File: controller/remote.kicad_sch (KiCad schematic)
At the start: 11 parts, among them J1 Conn_01x03, U6 MC130VX

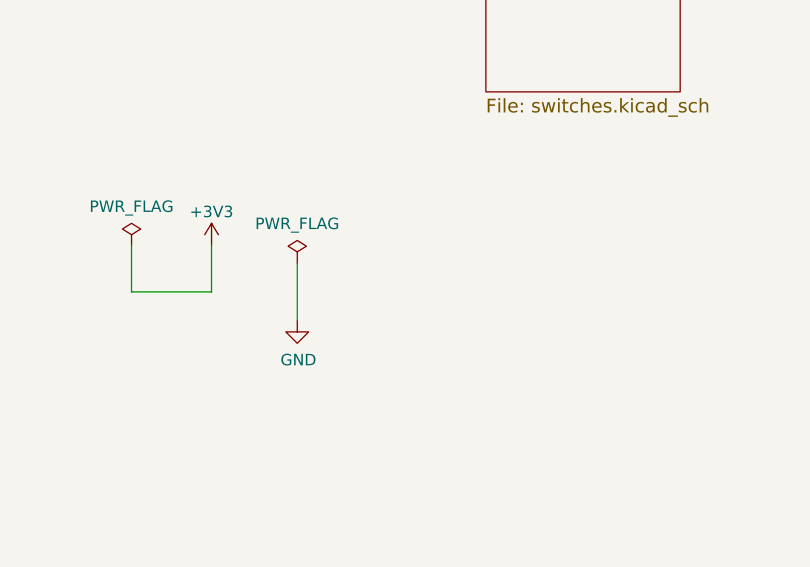
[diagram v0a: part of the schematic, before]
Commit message: Add debug connector.
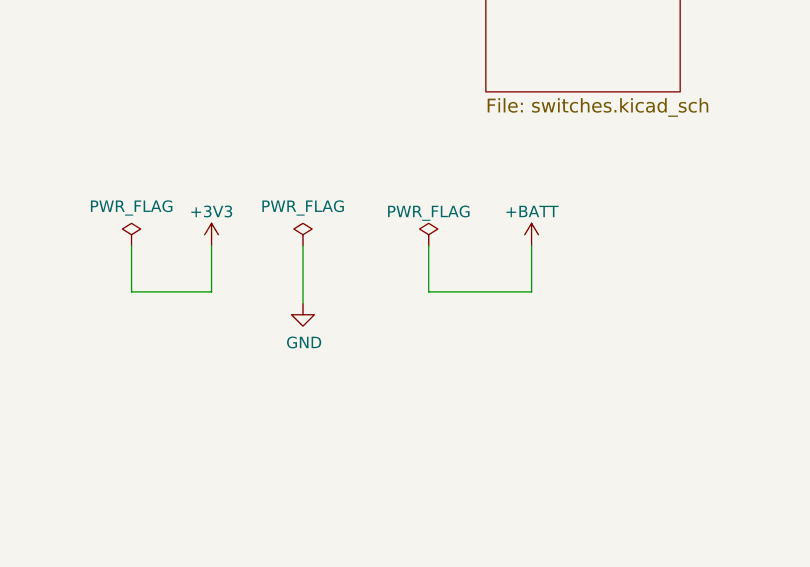
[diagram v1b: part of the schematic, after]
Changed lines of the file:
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@@
     (stroke (width 0) (type default))
   )
-  (wire (pts (xy 123.825 66.675) (xy 123.825 60.325))
+  (wire (pts (xy 149.86 63.5) (xy 138.43 63.5))
+    (stroke (width 0) (type default))
+  )
+  (wire (pts (xy 124.46 64.77) (xy 124.46 58.42))
     (stroke (width 0) (type default))
   )
@@
     (stroke (width 0) (type default))
   )
+  (wire (pts (xy 149.86 58.42) (xy 149.86 63.5))
+    (stroke (width 0) (type default))
+  )
   (wire (pts (xy 41.91 86.36) (xy 41.91 96.52))
     (stroke (width 0) (type default))
@@
   )
   (wire (pts (xy 41.91 45.72) (xy 46.99 45.72))
+    (stroke (width 0) (type default))
+  )
+  (wire (pts (xy 138.43 63.5) (xy 138.43 58.42))
     (stroke (width 0) (type default))
   )
@@
     )
   )
-  (symbol (lib_id "power:PWR_FLAG") (at 123.825 60.325 0) (unit 1)
-    (in_bom yes) (on_board yes) (dnp no)
-    (property "Reference" "#FLG0102" (at 123.825 58.42 0)
-      (effects (font (size 1.27 1.27)) hide)
-    )
-    (property "Value" "PWR_FLAG" (at 123.825 55.9308 0)
-      (effects (font (size 1.27 1.27)))
-    )
-    (property "Footprint" "" (at 123.825 60.325 0)
-      (effects (font (size 1.27 1.27)) hide)
-    )
-    (property "Datasheet" "~" (at 123.825 60.325 0)
+  (symbol (lib_id "power:PWR_FLAG") (at 124.46 58.42 0) (unit 1)
+    (in_bom yes) (on_board yes) (dnp no)
+    (property "Reference" "#FLG0102" (at 124.46 56.515 0)
+      (effects (font (size 1.27 1.27)) hide)
+    )
+    (property "Value" "PWR_FLAG" (at 124.46 54.0258 0)
+      (effects (font (size 1.27 1.27)))
+    )
+    (property "Footprint" "" (at 124.46 58.42 0)
+      (effects (font (size 1.27 1.27)) hide)
+    )
+    (property "Datasheet" "~" (at 124.46 58.42 0)
       (effects (font (size 1.27 1.27)) hide)
     )
@@
     )
   )
-  (symbol (lib_id "power:GND") (at 123.825 66.675 0) (unit 1)
-    (in_bom yes) (on_board yes) (dnp no)
-    (property "Reference" "#PWR0128" (at 123.825 73.025 0)
-      (effects (font (size 1.27 1.27)) hide)
-    )
-    (property "Value" "GND" (at 123.952 71.0692 0)
-      (effects (font (size 1.27 1.27)))
-    )
-    (property "Footprint" "" (at 123.825 66.675 0)
-      (effects (font (size 1.27 1.27)) hide)
-    )
-    (property "Datasheet" "" (at 123.825 66.675 0)
+  (symbol (lib_id "power:GND") (at 124.46 64.77 0) (unit 1)
+    (in_bom yes) (on_board yes) (dnp no)
+    (property "Reference" "#PWR0128" (at 124.46 71.12 0)
+      (effects (font (size 1.27 1.27)) hide)
+    )
+    (property "Value" "GND" (at 124.587 69.1642 0)
+      (effects (font (size 1.27 1.27)))
+    )
+    (property "Footprint" "" (at 124.46 64.77 0)
+      (effects (font (size 1.27 1.27)) hide)
+    )
+    (property "Datasheet" "" (at 124.46 64.77 0)
       (effects (font (size 1.27 1.27)) hide)
     )
@@
     )
   )
+  (symbol (lib_id "power:+BATT") (at 149.86 58.42 0) (unit 1)
+    (in_bom yes) (on_board yes) (dnp no) (fields_autoplaced)
+    (property "Reference" "#PWR019" (at 149.86 62.23 0)
+      (effects (font (size 1.27 1.27)) hide)
+    )
+    (property "Value" "+BATT" (at 149.86 54.61 0)
+      (effects (font (size 1.27 1.27)))
+    )
+    (property "Footprint" "" (at 149.86 58.42 0)
+      (effects (font (size 1.27 1.27)) hide)
+    )
+    (property "Datasheet" "" (at 149.86 58.42 0)
+      (effects (font (size 1.27 1.27)) hide)
+    )
+    (pin "1")
+    (instances
+      (project "remote"
+        (path "/0776e334-fbf5-4a46-a47e-c7e0521e2a6b"
+          (reference "#PWR019") (unit 1)
+        )
+      )
+    )
+  )
   (symbol (lib_id "Connector_Generic:Conn_01x03") (at 33.02 99.06 0) (mirror y) (unit 1)
     (in_bom yes) (on_board yes) (dnp no) (fields_autoplaced)
@@
         )
       )
+    )
+  )
+  (symbol (lib_id "power:PWR_FLAG") (at 138.43 58.42 0) (unit 1)
+    (in_bom yes) (on_board yes) (dnp no) (fields_autoplaced)
+    (property "Reference" "#FLG01" (at 138.43 56.515 0)
+      (effects (font (size 1.27 1.27)) hide)
+    )
+    (property "Value" "PWR_FLAG" (at 138.43 54.61 0)
+      (effects (font (size 1.27 1.27)))
+    )
+    (property "Footprint" "" (at 138.43 58.42 0)
+      (effects (font (size 1.27 1.27)) hide)
+    )
+    (property "Datasheet" "~" (at 138.43 58.42 0)
+      (effects (font (size 1.27 1.27)) hide)
+    )
+    (pin "1")
+    (instances
+      (project "remote"
+        (path "/0776e334-fbf5-4a46-a47e-c7e0521e2a6b"
+          (reference "#FLG01") (unit 1)
+        )
+      )

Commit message: Work on routing.
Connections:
- net +3V3: no longer C1.1
- net GND: no longer C1.2
- net at R1.1, R3.1, U6.GND (2): now also C1.1
- net at R2.1, R4.1, U6.VDD (1): now also C1.2
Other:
- moved on the sheet: C1, R1, R2, R3, R4

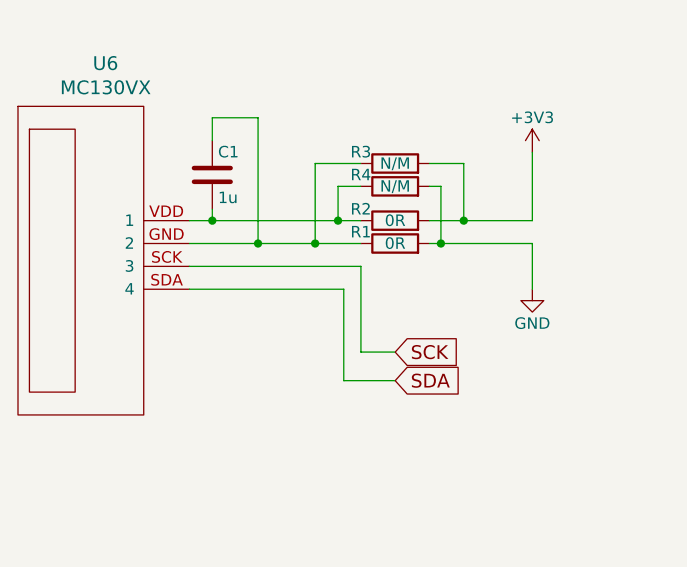
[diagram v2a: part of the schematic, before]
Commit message: Complete routing.
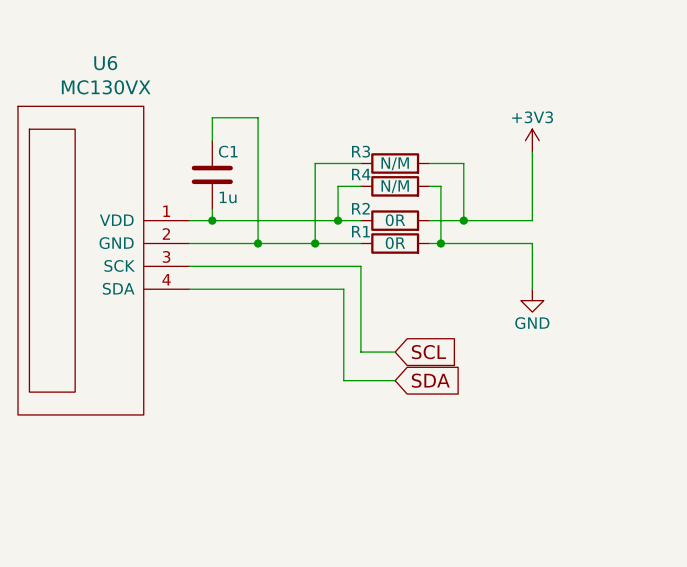
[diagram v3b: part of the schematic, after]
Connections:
- net SDA: now also U6.4 (SDA); no longer U6.SDA (4)
- net at C1.1, R1.1, R3.1: now also U6.2 (GND); no longer U6.GND (2)
- net at C1.2, R2.1, R4.1: now also U6.1 (VDD); no longer U6.VDD (1)
- removed net SCK: U6.SCK (3)
- new net SCL: U6.3 (SCK)
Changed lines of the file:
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@@
     )
   )
-  (global_label "SCK" (shape input) (at 62.23 57.785 0)
+  (global_label "SCL" (shape input) (at 62.23 57.785 0)
     (effects (font (size 1.524 1.524)) (justify left))
     (property "Intersheetrefs" "${INTERSHEET_REFS}" (at 62.23 57.785 0)
@@
       (effects (font (size 1.524 1.524)))
     )
-    (pin "GND")
-    (pin "SCK")
-    (pin "SDA")
-    (pin "VDD")
+    (pin "2")
+    (pin "3")
+    (pin "4")
+    (pin "1")
     (instances
       (project "remote"

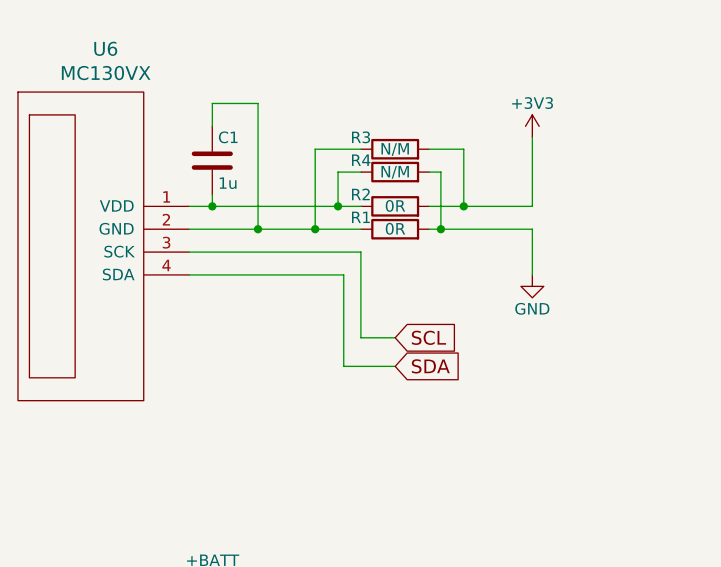
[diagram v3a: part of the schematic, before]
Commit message: Fix capacitor values.
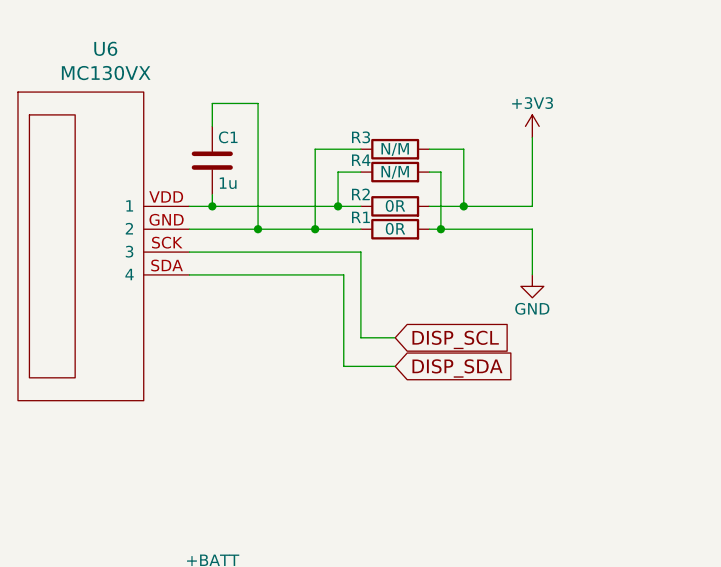
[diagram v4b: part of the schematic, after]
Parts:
- C1: footprint Capacitor_SMD:C_0805_2012Metric -> Capacitor_SMD:C_0603_1608Metric
- R1, R2: footprint Capacitor_SMD:C_0603_1608Metric -> Resistor_SMD:R_0603_1608Metric
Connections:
- net at C1.1, R1.1, R3.1: now also U6.GND (2); no longer U6.2 (GND)
- net at C1.2, R2.1, R4.1: now also U6.VDD (1); no longer U6.1 (VDD)
- removed net SCL: U6.3 (SCK)
- removed net SDA: U6.4 (SDA)
- new net DISP_SCL: U6.SCK (3)
- new net DISP_SDA: U6.SDA (4)

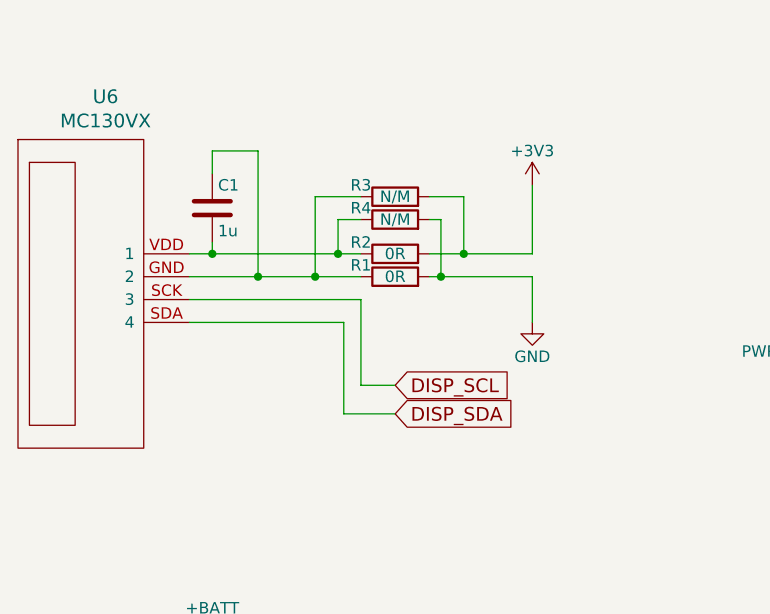
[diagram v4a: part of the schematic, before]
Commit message: Add switches, regulator, etc.
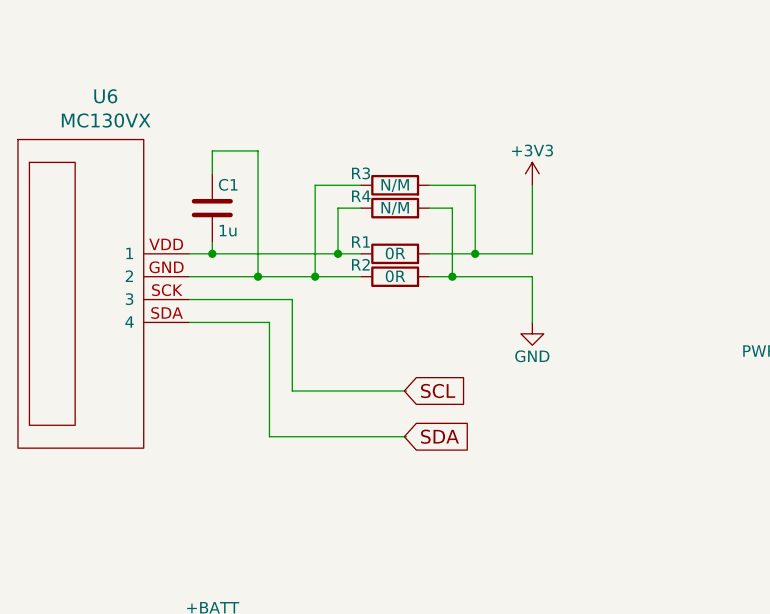
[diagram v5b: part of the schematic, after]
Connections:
- net +3V3: now also R1.2; no longer R2.2
- net GND: now also R2.2; no longer R1.2
- net at C1.1, R3.1, U6.GND (2): now also R2.1; no longer R1.1
- net at C1.2, R4.1, U6.VDD (1): now also R1.1; no longer R2.1
- net DISP_SCL renamed SCL
- net DISP_SDA renamed SDA
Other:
- moved on the sheet: R1, R2, R3, R4

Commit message: Finish routing.
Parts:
- removed U6: MC130VX, Remote:Display_OLED_4pin_I2C, symbol oled:OLED_4pin_I2C
- added J7: MC130VX, Connector_PinSocket_2.54mm:PinSocket_1x04_P2.54mm_Vertical, symbol Connector_Generic:Conn_01x04
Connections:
- net SCL: now also J7.3 (Pin_3)
- net SDA: now also J7.4 (Pin_4)
- net at C1.1, R2.1, R3.1: now also J7.2 (Pin_2)
- net at C1.2, R1.1, R4.1: now also J7.1 (Pin_1)
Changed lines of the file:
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@@
 	(global_label "SDA"
 		(shape input)
-		(at 63.246 63.5 0)
+		(at 63.5 63.5 0)
 		(effects
 			(font
@@
 		)
 		(property "Intersheetrefs" "${INTERSHEET_REFS}"
-			(at 63.246 63.5 0)
+			(at 63.5 63.5 0)
 			(effects
 				(font
@@
 	(global_label "SCL"
 		(shape input)
-		(at 63.246 58.42 0)
+		(at 63.5 58.42 0)
 		(effects
 			(font
@@
 		)
 		(property "Intersheetrefs" "${INTERSHEET_REFS}"
-			(at 63.246 58.42 0)
+			(at 63.5 58.42 0)
 			(effects
 				(font
@@
 				(path "/0776e334-fbf5-4a46-a47e-c7e0521e2a6b"
 					(reference "#PWR0128")
-					(unit 1)
-				)
-			)
-		)
-	)
-	(symbol
-		(lib_id "oled:OLED_4pin_I2C")
-		(at 27.94 43.18 90)
-		(mirror x)
-		(unit 1)
-		(exclude_from_sim no)
-		(in_bom yes)
-		(on_board yes)
-		(dnp no)
-		(property "Reference" "U6"
-			(at 30.0482 25.7302 90)
-			(effects
-				(font
-					(size 1.524 1.524)
-				)
-			)
-		)
-		(property "Value" "MC130VX"
-			(at 30.0482 28.4226 90)
-			(effects
-				(font
-					(size 1.524 1.524)
-				)
-			)
-		)
-		(property "Footprint" "Remote:Display_OLED_4pin_I2C"
-			(at 27.94 43.18 0)
-			(effects
-				(font
-					(size 1.524 1.524)
-				)
-				(hide yes)
-			)
-		)
-		(property "Datasheet" ""
-			(at 27.94 43.18 0)
-			(effects
-				(font
-					(size 1.524 1.524)
-				)
-			)
-		)
-		(property "Description" ""
-			(at 27.94 43.18 0)
-			(effects
-				(font
-					(size 1.27 1.27)
-				)
-				(hide yes)
-			)
-		)
-		(pin "GND"
-		)
-		(pin "SCK"
-		)
-		(pin "SDA"
-		)
-		(pin "VDD"
-		)
-		(instances
-			(project "remote"
-				(path "/0776e334-fbf5-4a46-a47e-c7e0521e2a6b"
-					(reference "U6")
 					(unit 1)
 				)
@@
 					(unit 1)
 				)
+			)
+		)
+	)
+	(symbol
+		(lib_id "Connector_Generic:Conn_01x04")
+		(at 34.29 45.72 0)
+		(mirror y)
+		(unit 1)
+		(exclude_from_sim no)
+		(in_bom yes)
+		(on_board yes)
+		(dnp no)
+		(fields_autoplaced yes)
+		(property "Reference" "J7"
+			(at 34.29 36.83 0)
+			(effects
+				(font
+					(size 1.27 1.27)
+				)
+			)
+		)
+		(property "Value" "MC130VX"
+			(at 34.29 39.37 0)
+			(effects
+				(font
+					(size 1.27 1.27)
+				)
+			)
+		)
+		(property "Footprint" "Connector_PinSocket_2.54mm:PinSocket_1x04_P2.54mm_Vertical"
+			(at 34.29 45.72 0)
+			(effects
+				(font
+					(size 1.27 1.27)
+				)
+				(hide yes)
+			)
+		)
+		(property "Datasheet" "~"
+			(at 34.29 45.72 0)
+			(effects
+				(font
+					(size 1.27 1.27)
+				)
+				(hide yes)
+			)
+		)
+		(property "Description" "Generic connector, single row, 01x04, script generated (kicad-library-utils/schlib/autogen/connector/)"
+			(at 34.29 45.72 0)
+			(effects
+				(font
+					(size 1.27 1.27)
+				)
+				(hide yes)
+			)
+		)
+		(pin "4"
+		)
+		(pin "3"
+		)
+		(pin "2"
+		)
+		(pin "1"
+		)
+		(instances
+			(project "remote"
+				(path "/0776e334-fbf5-4a46-a47e-c7e0521e2a6b"
+					(reference "J7")
+					(unit 1)
+				)

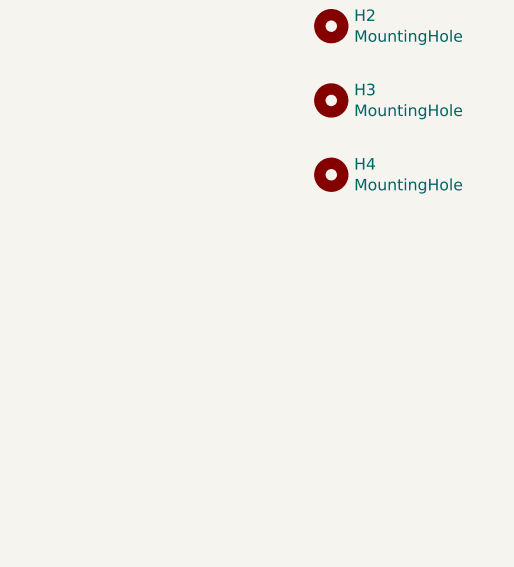
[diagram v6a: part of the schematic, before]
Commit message: Add nRF mounting screw.
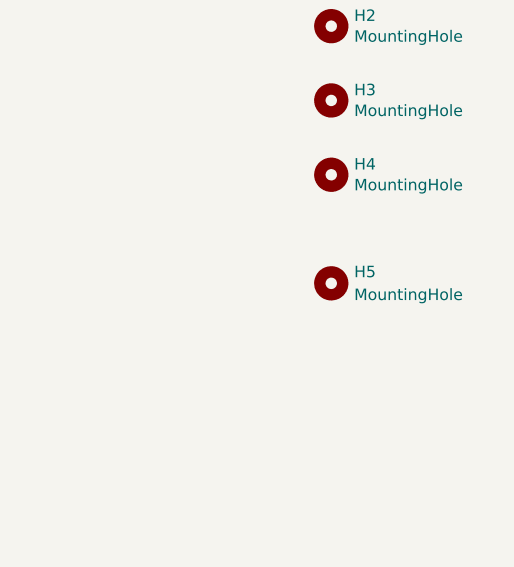
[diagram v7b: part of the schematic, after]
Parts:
- added H5: MountingHole, MountingHole:MountingHole_2.2mm_M2, symbol Mechanical:MountingHole
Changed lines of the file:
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@@
+	)
+	(symbol
+		(lib_id "Mechanical:MountingHole")
+		(at 261.62 55.88 0)
+		(unit 1)
+		(exclude_from_sim no)
+		(in_bom yes)
+		(on_board yes)
+		(dnp no)
+		(fields_autoplaced yes)
+		(property "Reference" "H5"
+			(at 264.16 54.6099 0)
+			(effects
+				(font
+					(size 1.27 1.27)
+				)
+				(justify left)
+			)
+		)
+		(property "Value" "MountingHole"
+			(at 264.16 57.1499 0)
+			(effects
+				(font
+					(size 1.27 1.27)
+				)
+				(justify left)
+			)
+		)
+		(property "Footprint" "MountingHole:MountingHole_2.2mm_M2"
+			(at 261.62 55.88 0)
+			(effects
+				(font
+					(size 1.27 1.27)
+				)
+				(hide yes)
+			)
+		)
+		(property "Datasheet" "~"
+			(at 261.62 55.88 0)
+			(effects
+				(font
+					(size 1.27 1.27)
+				)
+				(hide yes)
+			)
+		)
+		(property "Description" "Mounting Hole without connection"
+			(at 261.62 55.88 0)
+			(effects
+				(font
+					(size 1.27 1.27)
+				)
+				(hide yes)
+			)
+		)
+		(instances
+			(project "remote"
+				(path "/0776e334-fbf5-4a46-a47e-c7e0521e2a6b"
+					(reference "H5")
+					(unit 1)
+				)
+			)
+		)
 	)
 	(symbol
